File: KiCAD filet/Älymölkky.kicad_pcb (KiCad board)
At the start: 2 copper layers, 43 parts, among them P0.18_TP1 Conn_01x01_Male, U1 nRF52810-QCxx, X1 32MHz Crystal, X2 32.768 kHz Crystal

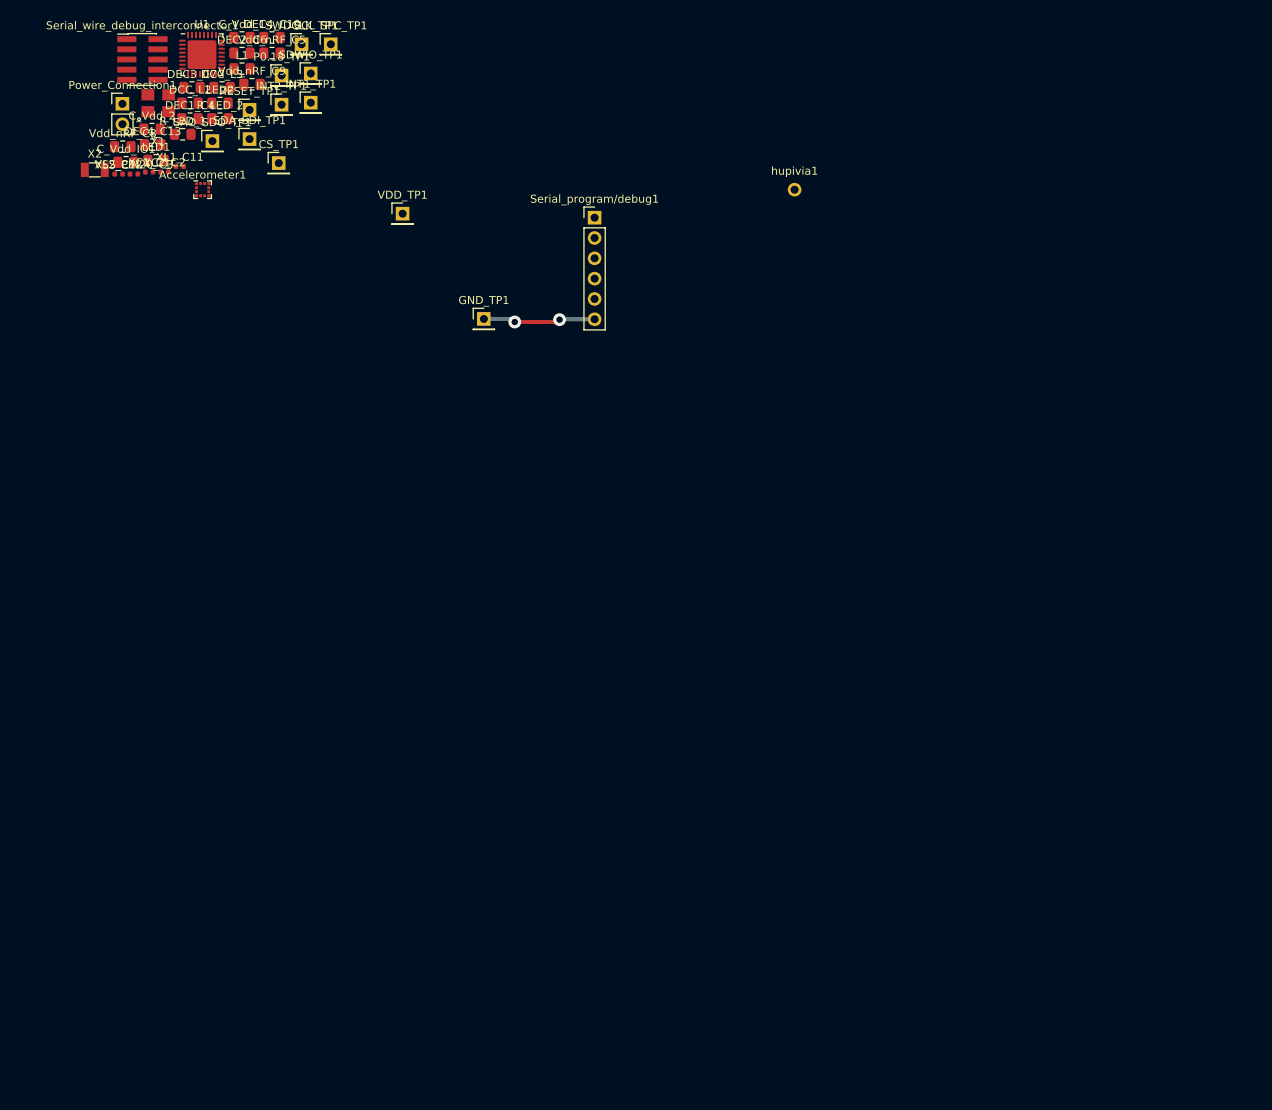
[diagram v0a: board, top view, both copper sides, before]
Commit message: Added fuse, modified nRF and LIS footprints and started layout work
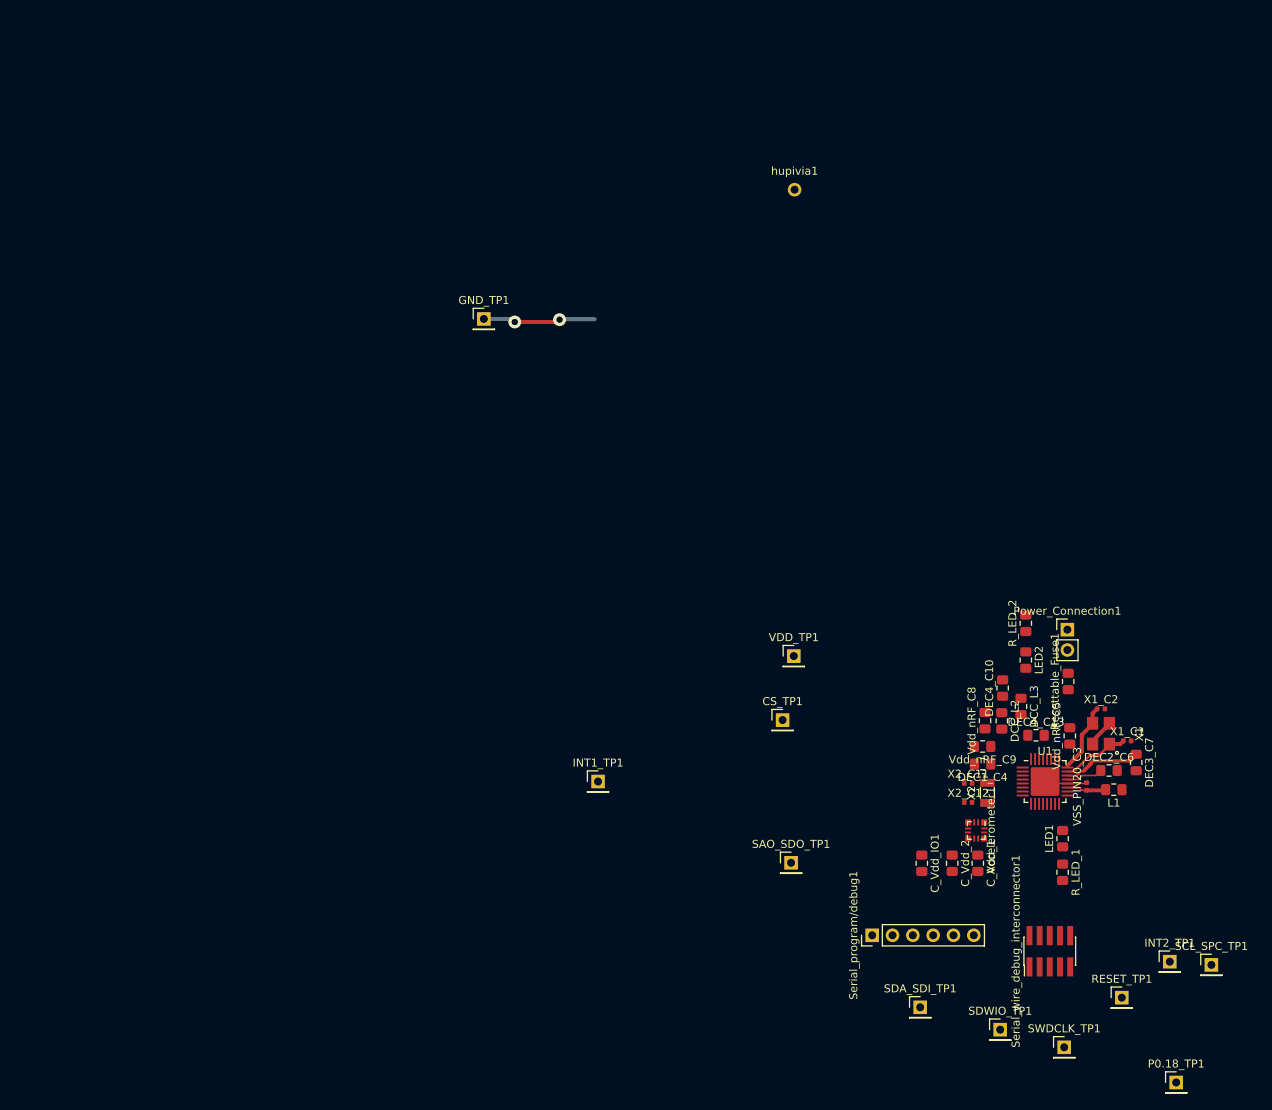
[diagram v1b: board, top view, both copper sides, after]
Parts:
- removed XC1_C1, XC2_C2, XL1_C11, XL2_C12: 12pF, Capacitor_SMD:C_0402_1005Metric
- added Resettable_Fuse1: Polyfuse, Resistor_SMD:R_0805_2012Metric_Pad1.15x1.40mm_HandSolder, F.Cu at (133.7, 81.5)
- added X1_C1: 12pF, Capacitor_SMD:C_0402_1005Metric, F.Cu at (141.1, 88.9)
- added X1_C2: 12pF, Capacitor_SMD:C_0402_1005Metric, F.Cu at (137.8, 84.9)
- added X2_C11: 12pF, Capacitor_SMD:C_0402_1005Metric, F.Cu at (121.2, 94.2)
- added X2_C12: 12pF, Capacitor_SMD:C_0402_1005Metric, F.Cu at (121.2, 96.6)
- Accelerometer1: footprint Package_LGA:LGA-12_2x2mm_P0.5mm -> Custom_footprints_alymolkky:LGA-12_2x2mm_P0.5mm
- U1: footprint Package_DFN_QFN:QFN-32-1EP_5x5mm_P0.5mm_EP3.6x3.6mm -> Custom_footprints_alymolkky:QFN-32-1EP_5x5mm_P0.5mm_EP3.6x3.6mm
- moved P0.18_TP1 168.4 mm to (147.2, 131.6)
- moved SCL_SPC_TP1 159.2 mm to (151.6, 116.9)
- moved Serial_wire_debug_interconnector1 159.0 mm to (131.4, 115.2), turned to 90 degrees
- moved SWDCLK_TP1 157.5 mm to (133.2, 127.2)
- moved RESET_TP1 155.6 mm to (140.4, 121.0)
- moved INT2_TP1 154.3 mm to (146.4, 116.5)
- moved SDWIO_TP1 147.4 mm to (125.2, 125.0)
- moved DEC3_C7 145.1 mm to (142.2, 91.6), turned to 270 degrees
- moved R_LED_1 143.5 mm to (133.0, 105.3), turned to 270 degrees
- moved X1 141.8 mm to (137.8, 88.0), turned to 90 degrees
- moved VSS_PIN20_C3 141.6 mm to (136.0, 94.6), turned to 90 degrees
- moved LED1 141.5 mm to (133.0, 101.1), turned to 90 degrees
- moved L1 141.4 mm to (139.4, 95.0), turned to 180 degrees
- moved DEC2_C6 140.7 mm to (138.8, 92.6)
- moved U1 139.1 mm to (130.8, 94.0)
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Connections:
- net /~P0.04 renamed /~RX1
- net /~P0.05 renamed /~TX0
- net /~P0.18 renamed /~SWO
- GND_TP1 pad 1: Earth -> /~GND
- Power_Connection1 pad 2: VDD -> Net-(Power_Connection1-Pad2)
- hupivia1 pad 1: Earth -> /~GND
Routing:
- net /~GND: track 0.00 -> 14.1 mm, vias 0 -> 2
- net Net-(DEC3_C7-Pad1): track 0.00 -> 9.41 mm
- net Net-(U1-Pad24): track 0.00 -> 8.86 mm
- net Net-(U1-Pad23): track 0.00 -> 8.64 mm
- net Earth: track 14.1 -> 8.81 mm, vias 2 -> 0
- net Net-(L1-Pad2): track 0.00 -> 4.95 mm
- net Net-(DEC2_C6-Pad1): track 0.00 -> 4.63 mm

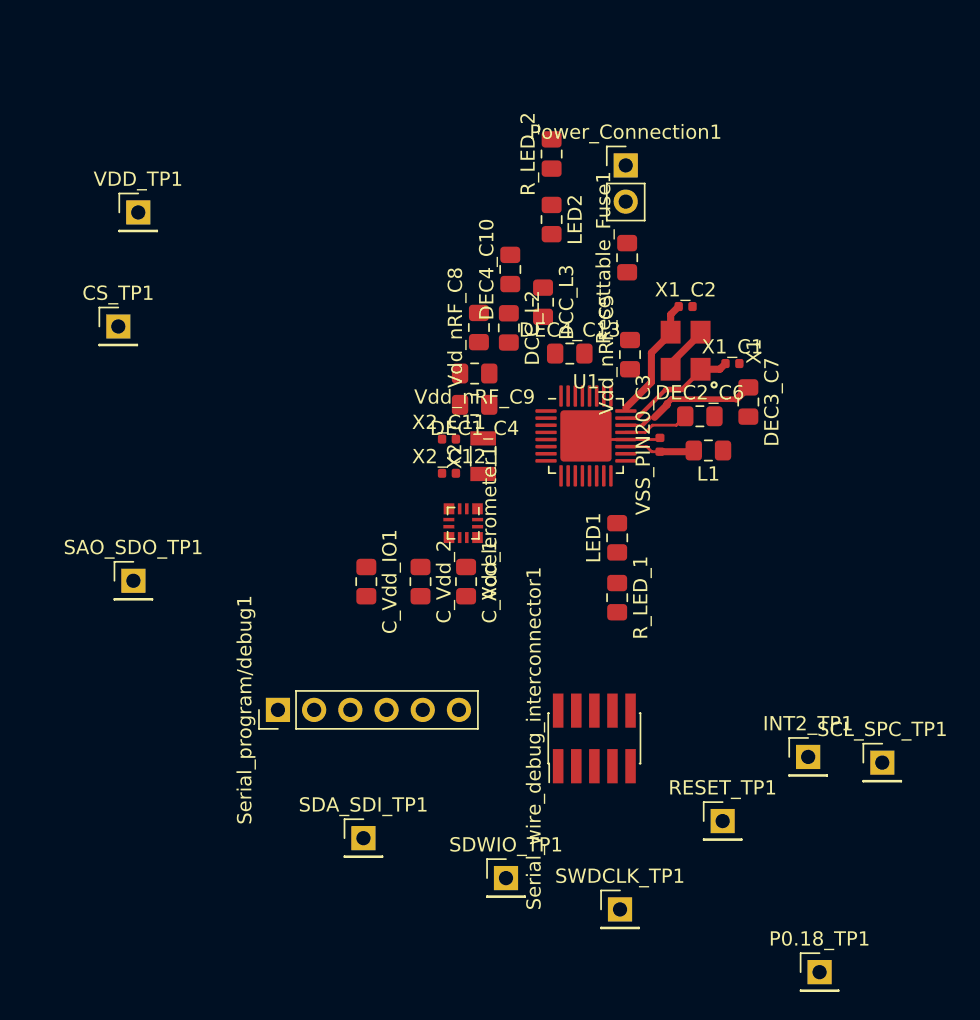
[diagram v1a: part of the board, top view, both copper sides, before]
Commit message: Added more traces, shifted one pin's place and will shift more soon
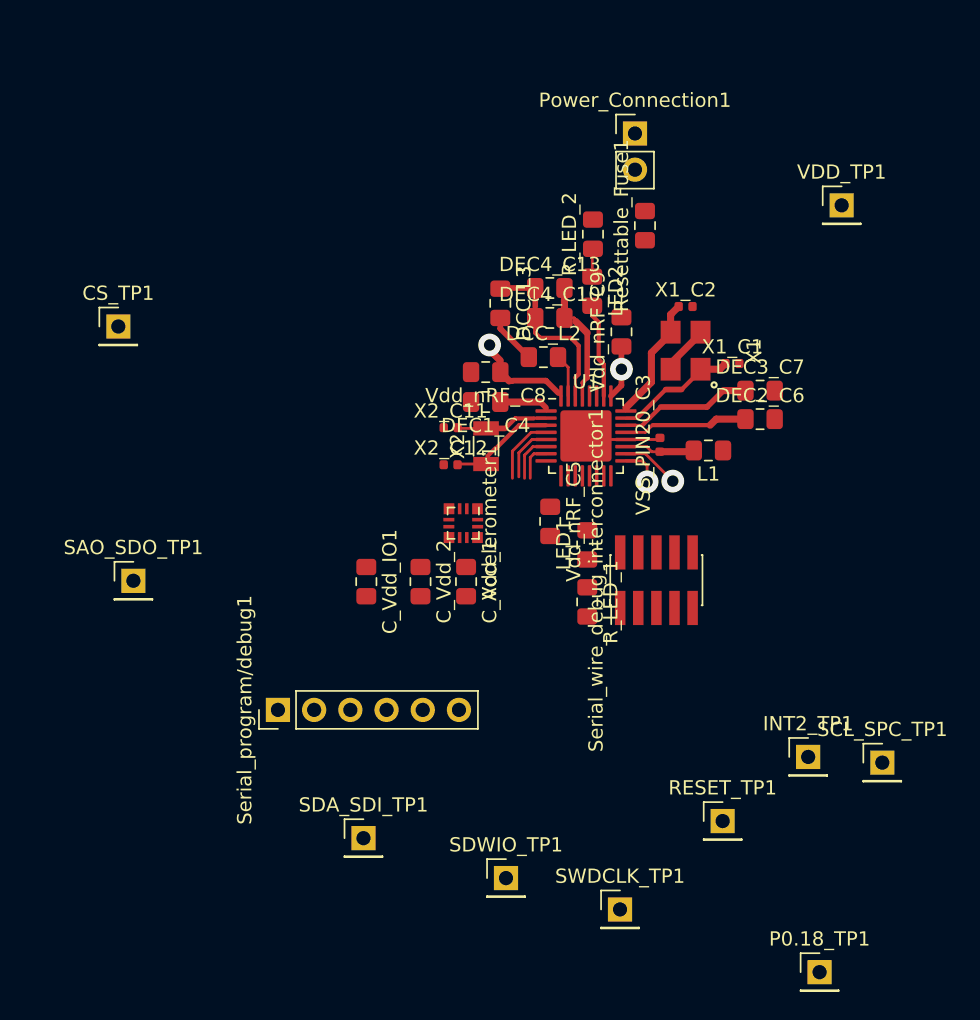
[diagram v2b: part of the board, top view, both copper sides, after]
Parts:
- moved VDD_TP1 49.4 mm to (148.8, 77.8)
- moved Vdd_nRF_C5 13.0 mm to (128.3, 100.0), turned to 270 degrees
- moved Serial_wire_debug_interconnector1 11.9 mm to (135.8, 104.1)
- moved Vdd_nRF_C9 10.7 mm to (133.3, 86.7), turned to 90 degrees
- moved R_LED_2 6.33 mm to (131.3, 79.8)
- moved LED2 5.78 mm to (131.2, 83.8)
- moved DEC4_C13 4.81 mm to (128.3, 83.6)
- moved DEC4_C10 4.39 mm to (128.3, 85.7), turned to 0 degrees
- moved DEC2_C6 4.23 mm to (143.0, 92.8)
- moved DCC_L2 3.18 mm to (127.8, 88.5), turned to 0 degrees
- moved Vdd_nRF_C8 3.16 mm to (123.8, 89.5), turned to 180 degrees
- moved DCC_L3 3.00 mm to (124.8, 84.7)
- moved Resettable_Fuse1 2.57 mm to (134.9, 79.2)
- moved Power_Connection1 2.33 mm to (134.2, 72.8)
- moved LED1 2.16 mm to (130.9, 101.6)
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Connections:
- U1 pad 14: /~SWO -> Net-(LED1-Pad2)
- U1 pad 15: Net-(LED1-Pad2) -> /~SWO
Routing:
- net Net-(DCC_L3-Pad1): track 0.00 -> 12.7 mm
- net VDD: track 0.00 -> 11.0 mm, vias 0 -> 2
- net Earth: track 8.81 -> 17.7 mm
- net Net-(U1-Pad3): track 0.00 -> 7.62 mm
- net Net-(LED2-Pad2): track 0.00 -> 6.67 mm
- net Net-(U1-Pad2): track 0.00 -> 6.53 mm
- net /~RX1: track 0.00 -> 4.81 mm
- net Net-(DEC2_C6-Pad1): track 4.63 -> 8.78 mm
- net /~SWDIO: track 0.00 -> 4.09 mm, vias 0 -> 1
- net /~TX0: track 0.00 -> 3.99 mm
- net Net-(DEC1_C4-Pad1): track 0.00 -> 3.60 mm
- net Net-(DCC_L2-Pad1): track 0.00 -> 3.58 mm
- net /~INT1: track 0.00 -> 3.38 mm
- net Net-(DCC_L2-Pad2): track 0.00 -> 3.02 mm
- net /~SWDCLK: track 0.00 -> 2.76 mm, vias 0 -> 1
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
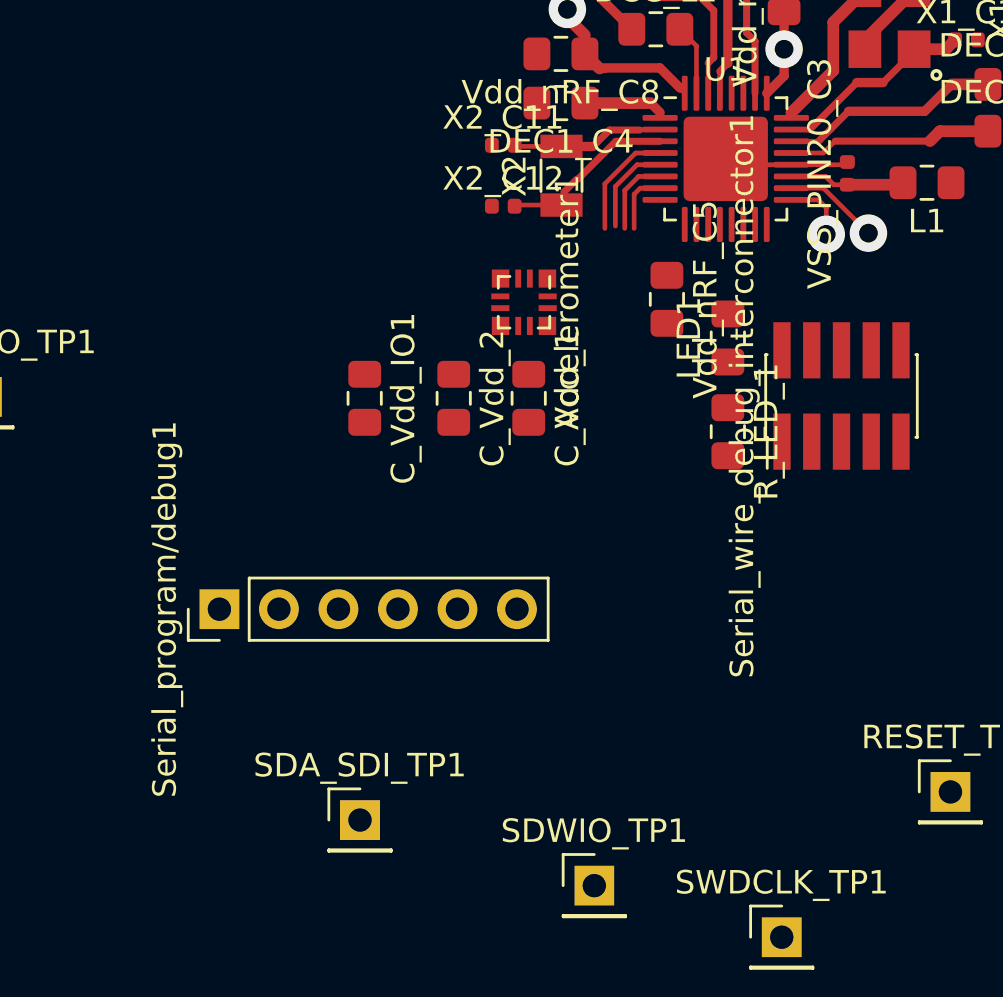
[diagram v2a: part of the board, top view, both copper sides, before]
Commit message: Reorganized more pins, drew LIS traces
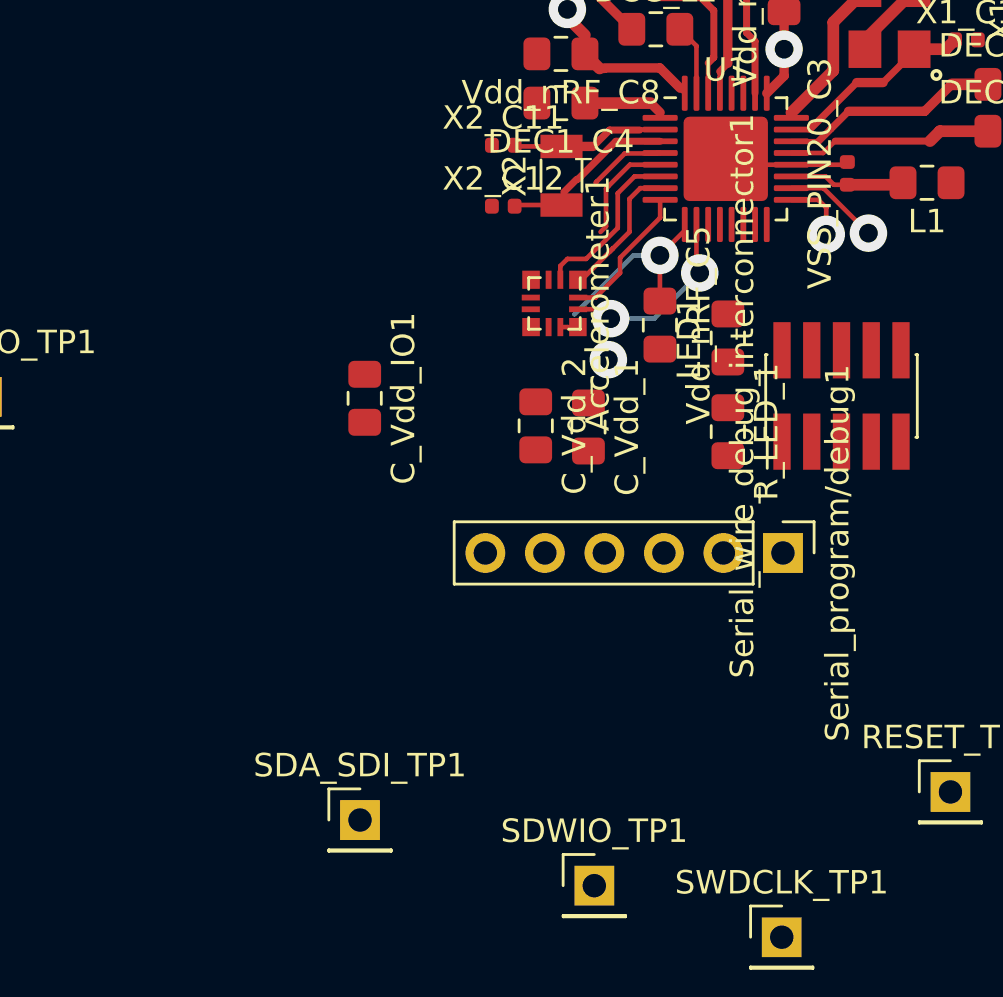
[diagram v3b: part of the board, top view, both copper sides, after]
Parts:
- moved Serial_program/debug1 24.2 mm to (133.2, 110.8), turned to 270 degrees
- moved C_Vdd_2 3.69 mm to (122.7, 105.4)
- moved C_Vdd_1 2.83 mm to (125.0, 105.4)
- moved Accelerometer1 1.30 mm to (123.5, 100.2)
- moved Vdd_nRF_C5 1.14 mm to (128.0, 101.1)
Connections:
- U1 pad 10: /~SDA_SDI -> /~INT2
- U1 pad 11: /~SAO_SDO -> Net-(LED1-Pad2)
- U1 pad 12: /~SCL_SPC -> /~RX1
- U1 pad 13: Net-(U1-Pad13) -> /~TX0
- U1 pad 14: Net-(LED1-Pad2) -> Net-(U1-Pad14)
- U1 pad 4: /~RX1 -> /~SDA_SDI
- U1 pad 5: /~TX0 -> /~SAO_SDO
- U1 pad 6: /~INT1 -> /~CS
- U1 pad 7: /~INT2 -> /~SCL_SPC
- U1 pad 8: /~CS -> /~INT1
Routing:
- net VDD: track 11.0 -> 20.3 mm, vias 2 -> 4
- net /~CS: track 0.00 -> 7.30 mm
- net /~SCL_SPC: track 0.00 -> 6.18 mm
- net /~INT2: track 2.68 -> 8.79 mm, vias 0 -> 2
- net /~RX1: track 4.81 -> 0.00 mm
- net /~SAO_SDO: track 0.00 -> 4.68 mm
- net /~TX0: track 3.99 -> 0.00 mm
- net /~SDA_SDI: track 0.00 -> 3.29 mm
- net /~INT1: track 3.38 -> 6.05 mm
